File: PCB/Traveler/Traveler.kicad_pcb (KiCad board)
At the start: 2 copper layers, 5 parts, among them J1 Conn_01x06_motFL, J2 Conn_01x06_motFR, J3 Conn_01x06_motBL, J4 Conn_01x06_motBR, U1 ESP32-DEVKITC

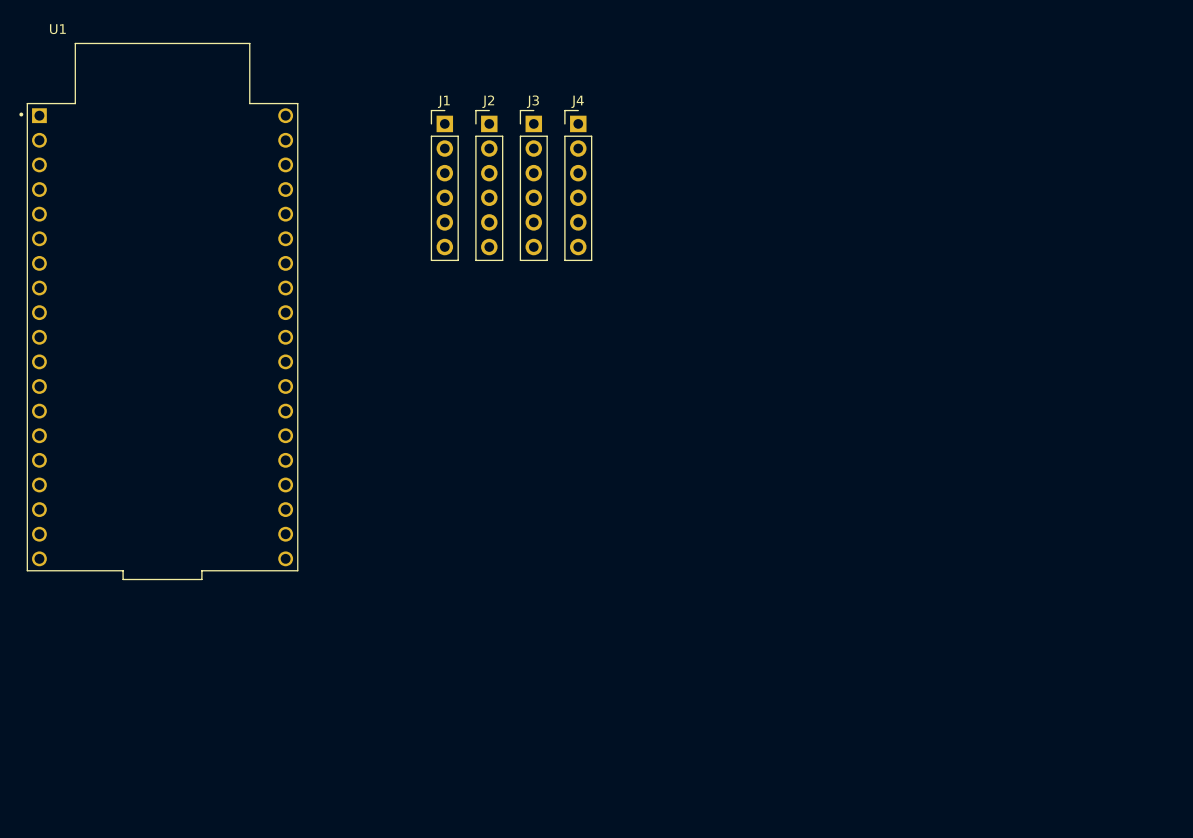
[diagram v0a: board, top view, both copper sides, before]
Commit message: Finition de pcb, prèt pour verification
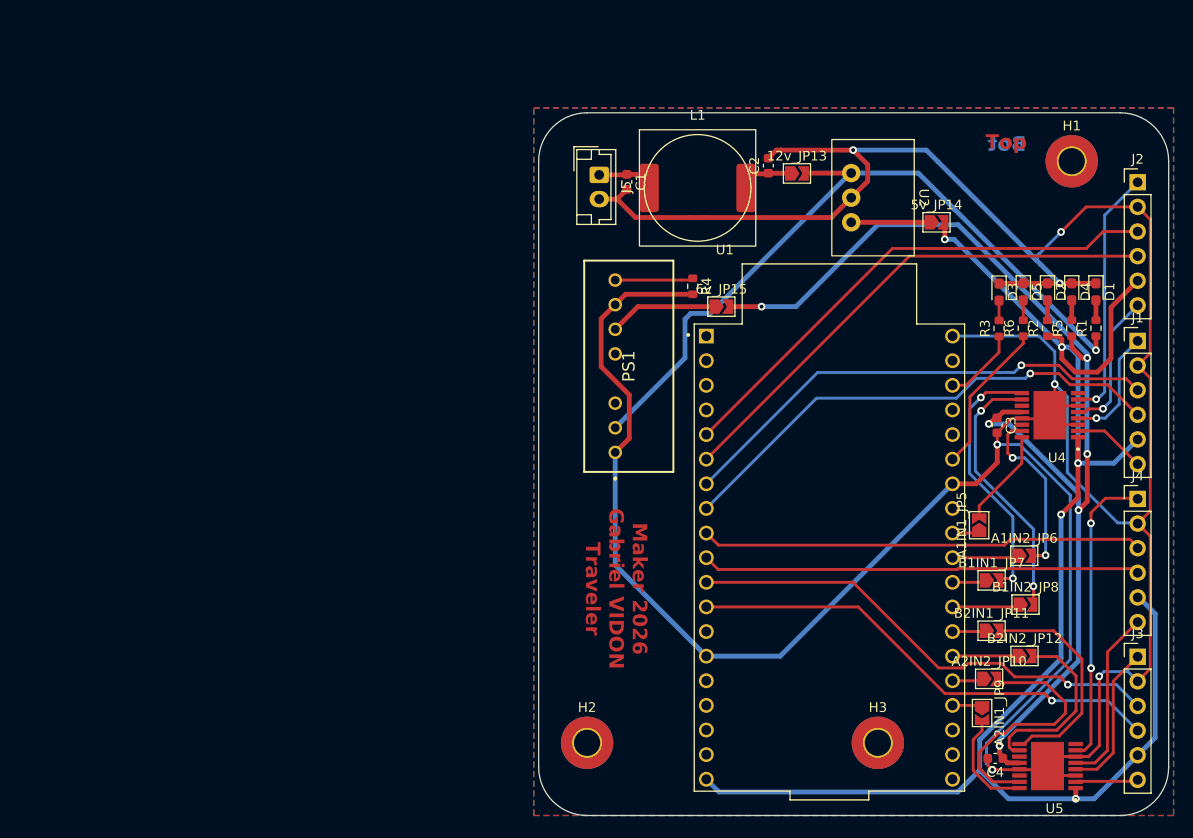
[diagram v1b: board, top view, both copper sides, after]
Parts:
- added 12v_JP13: SolderJumper_2_Open, Jumper:SolderJumper-2_P1.3mm_Open_TrianglePad1.0x1.5mm, F.Cu at (144.2, 48.8)
- added 5v_JP14: SolderJumper_2_Open, Jumper:SolderJumper-2_P1.3mm_Open_TrianglePad1.0x1.5mm, F.Cu at (158.5, 53.8)
- added 6v_JP15: SolderJumper_2_Open, Jumper:SolderJumper-2_P1.3mm_Open_TrianglePad1.0x1.5mm, F.Cu at (136.3, 62.5)
- added A1IN1_JP5: SolderJumper_2_Open, Jumper:SolderJumper-2_P1.3mm_Open_TrianglePad1.0x1.5mm, F.Cu at (162.9, 85.0)
- added A1IN2_JP6: SolderJumper_2_Open, Jumper:SolderJumper-2_P1.3mm_Open_TrianglePad1.0x1.5mm, F.Cu at (167.6, 88.2)
- added A2IN1_JP9: SolderJumper_2_Open, Jumper:SolderJumper-2_P1.3mm_Open_TrianglePad1.0x1.5mm, F.Cu at (163.2, 104.4)
- added A2IN2_JP10: SolderJumper_2_Open, Jumper:SolderJumper-2_P1.3mm_Open_TrianglePad1.0x1.5mm, F.Cu at (164.0, 100.9)
- added B1IN1_JP7: SolderJumper_2_Open, Jumper:SolderJumper-2_P1.3mm_Open_TrianglePad1.0x1.5mm, F.Cu at (164.2, 90.7)
- added B1IN2_JP8: SolderJumper_2_Open, Jumper:SolderJumper-2_P1.3mm_Open_TrianglePad1.0x1.5mm, F.Cu at (167.7, 93.2)
- added B2IN1_JP11: SolderJumper_2_Open, Jumper:SolderJumper-2_P1.3mm_Open_TrianglePad1.0x1.5mm, F.Cu at (164.2, 95.9)
- added B2IN2_JP12: SolderJumper_2_Open, Jumper:SolderJumper-2_P1.3mm_Open_TrianglePad1.0x1.5mm, F.Cu at (167.6, 98.5)
- added C1: 4.7u, Capacitor_SMD:C_0603_1608Metric, F.Cu at (126.6, 49.6)
- added C2: 4.7u, Capacitor_SMD:C_0603_1608Metric, F.Cu at (141.2, 48.0)
- added C3: 100n, Capacitor_SMD:C_0603_1608Metric, F.Cu at (164.8, 74.8)
- added C4: 100n, Capacitor_SMD:C_0603_1608Metric, F.Cu at (164.6, 109.1)
- added D1: LED_12v, LED_SMD:LED_0603_1608Metric_Pad1.05x0.95mm_HandSolder, F.Cu at (175.0, 61.0)
- added D2: LED_5v, LED_SMD:LED_0603_1608Metric_Pad1.05x0.95mm_HandSolder, F.Cu at (170.0, 61.0)
- added D3: LED_conn_bt, LED_SMD:LED_0603_1608Metric_Pad1.05x0.95mm_HandSolder, F.Cu at (165.0, 61.0)
- added D4: LED_6v, LED_SMD:LED_0603_1608Metric_Pad1.05x0.95mm_HandSolder, F.Cu at (172.5, 61.0)
- added D5: LED_spare1, LED_SMD:LED_0603_1608Metric_Pad1.05x0.95mm_HandSolder, F.Cu at (167.5, 61.0)
- added H1: MountingHole_Pad, MountingHole:MountingHole_2.7mm_Pad_TopBottom, F.Cu at (172.5, 47.5)
- added H2: MountingHole_Pad, MountingHole:MountingHole_2.7mm_Pad_TopBottom, F.Cu at (122.5, 107.5)
- added H3: MountingHole_Pad, MountingHole:MountingHole_2.7mm_Pad_TopBottom, F.Cu at (152.5, 107.5)
- added J5: Conn_batt, Connector_JST:JST_EH_B2B-EH-A_1x02_P2.50mm_Vertical, F.Cu at (123.8, 48.9)
- added L1: 10u, Capa:capa1, F.Cu at (133.9, 50.2)
- added PS1: 17791063215, 17791063215:17791063215, F.Cu at (125.4, 77.5)
- added R1: 4.7k, Resistor_SMD:R_0603_1608Metric, F.Cu at (175.0, 64.7)
- added R2: 1.2k, Resistor_SMD:R_0603_1608Metric, F.Cu at (170.0, 64.7)
- added R3: 120, Resistor_SMD:R_0603_1608Metric, F.Cu at (165.0, 64.7)
- added R4: 21.5k, Resistor_SMD:R_0603_1608Metric, F.Cu at (133.4, 60.4)
- added R5: 2.2k, Resistor_SMD:R_0603_1608Metric, F.Cu at (172.5, 64.7)
- added R6: 120, Resistor_SMD:R_0603_1608Metric, F.Cu at (167.5, 64.7)
- added U2: 12v-5v, Conv_dc-dc:173950x78, F.Cu at (159.7, 51.3)
- added U4: DRV8411APWPR, DRV8411APWPR:IC_DRV8411APWPR, F.Cu at (170.2, 73.7)
- added U5: DRV8411APWPR, DRV8411APWPR:IC_DRV8411APWPR, F.Cu at (170.0, 109.9)
- moved J3 83.1 mm to (179.3, 98.6)
- moved J1 74.9 mm to (179.3, 66.0)
- moved U1 72.5 mm to (147.5, 88.4)
- moved J4 69.5 mm to (179.3, 82.3)
- moved J2 67.2 mm to (179.3, 49.7)
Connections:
- J1 pad 1: unconnected-(J1-Pin_1-Pad1) -> /A1OUT2
- J1 pad 2: unconnected-(J1-Pin_2-Pad2) -> GND
- J1 pad 3: unconnected-(J1-Pin_3-Pad3) -> /Enc_A1_A
- J1 pad 4: unconnected-(J1-Pin_4-Pad4) -> /Enc_A1_B
- J1 pad 5: unconnected-(J1-Pin_5-Pad5) -> 5V
- J1 pad 6: unconnected-(J1-Pin_6-Pad6) -> /A1OUT1
- J2 pad 1: unconnected-(J2-Pin_1-Pad1) -> /B1OUT1
- J2 pad 2: unconnected-(J2-Pin_2-Pad2) -> GND
- J2 pad 3: unconnected-(J2-Pin_3-Pad3) -> /Enc_B1_A
- J2 pad 4: unconnected-(J2-Pin_4-Pad4) -> /Enc_B1_B
- J2 pad 5: unconnected-(J2-Pin_5-Pad5) -> 5V
- J2 pad 6: unconnected-(J2-Pin_6-Pad6) -> /B1OUT2
- J3 pad 1: unconnected-(J3-Pin_1-Pad1) -> /A2OUT2
- J3 pad 2: unconnected-(J3-Pin_2-Pad2) -> GND
- J3 pad 3: unconnected-(J3-Pin_3-Pad3) -> /Enc_A2_A
- J3 pad 4: unconnected-(J3-Pin_4-Pad4) -> /Enc_A2_B
- J3 pad 5: unconnected-(J3-Pin_5-Pad5) -> 5V
- J3 pad 6: unconnected-(J3-Pin_6-Pad6) -> /A2OUT1
- J4 pad 1: unconnected-(J4-Pin_1-Pad1) -> /B2OUT1
- J4 pad 2: unconnected-(J4-Pin_2-Pad2) -> GND
- J4 pad 3: unconnected-(J4-Pin_3-Pad3) -> /Enc_B2_A
- J4 pad 4: unconnected-(J4-Pin_4-Pad4) -> /Enc_B2_B
- J4 pad 5: unconnected-(J4-Pin_5-Pad5) -> 5V
- J4 pad 6: unconnected-(J4-Pin_6-Pad6) -> /B2OUT2
- U1 pad 10: unconnected-(U1-IO26-Pad10) -> /Enc_B2_B
- U1 pad 11: unconnected-(U1-IO27-Pad11) -> /Enc_A2_A
- U1 pad 12: unconnected-(U1-IO14-Pad12) -> /Enc_A2_B
- U1 pad 14: unconnected-(U1-GND1-Pad14) -> GND
- U1 pad 19: unconnected-(U1-EXT_5V-Pad19) -> 5V
- U1 pad 23: unconnected-(U1-IO15-Pad23) -> Net-(A2IN1_JP9-A)
- U1 pad 24: unconnected-(U1-IO2-Pad24) -> Net-(A2IN2_JP10-A)
- U1 pad 25: unconnected-(U1-IO0-Pad25) -> Net-(B2IN2_JP12-A)
- U1 pad 26: unconnected-(U1-IO4-Pad26) -> Net-(B2IN1_JP11-A)
- U1 pad 27: unconnected-(U1-IO16-Pad27) -> Net-(B1IN2_JP8-A)
- U1 pad 28: unconnected-(U1-IO17-Pad28) -> Net-(B1IN1_JP7-A)
- U1 pad 29: unconnected-(U1-IO5-Pad29) -> Net-(A1IN2_JP6-A)
- U1 pad 30: unconnected-(U1-IO18-Pad30) -> Net-(A1IN1_JP5-A)
- U1 pad 31: unconnected-(U1-IO19-Pad31) -> LED_spare2
- U1 pad 32: unconnected-(U1-GND2-Pad32) -> GND
- U1 pad 33: unconnected-(U1-IO21-Pad33) -> LED_spare1
- U1 pad 36: unconnected-(U1-IO22-Pad36) -> LED_conn_bt
- U1 pad 38: unconnected-(U1-GND3-Pad38) -> GND
- U1 pad 5: unconnected-(U1-IO34-Pad5) -> /Enc_B1_A
- U1 pad 6: unconnected-(U1-IO35-Pad6) -> /Enc_B1_B
- U1 pad 7: unconnected-(U1-IO32-Pad7) -> /Enc_A1_A
- U1 pad 8: unconnected-(U1-IO33-Pad8) -> /Enc_A1_B
- U1 pad 9: unconnected-(U1-IO25-Pad9) -> /Enc_B2_A
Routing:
- net GND: track 0.00 -> 360.0 mm, vias 0 -> 7
- net 5V: track 0.00 -> 164.3 mm, vias 0 -> 5
- net 6V: track 0.00 -> 114.7 mm, vias 0 -> 6
- net 12V: track 0.00 -> 76.6 mm, vias 0 -> 1
- net /Enc_B1_A: track 0.00 -> 53.2 mm
- net /Enc_B1_B: track 0.00 -> 53.2 mm
- net /Enc_A1_B: track 0.00 -> 52.0 mm, vias 0 -> 1
- net /Enc_A1_A: track 0.00 -> 50.6 mm, vias 0 -> 1
- net /Enc_A2_A: track 0.00 -> 50.2 mm, vias 0 -> 1
- net /Enc_A2_B: track 0.00 -> 49.8 mm, vias 0 -> 1
- net /Enc_B2_A: track 0.00 -> 45.7 mm
- net /Enc_B2_B: track 0.00 -> 45.2 mm
- net /B2OUT1: track 0.00 -> 31.2 mm, vias 0 -> 2
- net B1IN2: track 0.00 -> 27.4 mm, vias 0 -> 2
- net B1IN1: track 0.00 -> 27.0 mm, vias 0 -> 2
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- added copper zone on B.Cu, net GND
- added copper zone on F.Cu, net GND
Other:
- board outline added: 65 x 72.5 mm
- board text added: "Bot"
- board text added: "Maker 2026 Gabriel VIDON Traveler"
- board text added: "Top"

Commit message: Vers 2 couches
A créer : une vers 4 couches, remplacer batt 12v vers 6v pour alim directement depuis batt
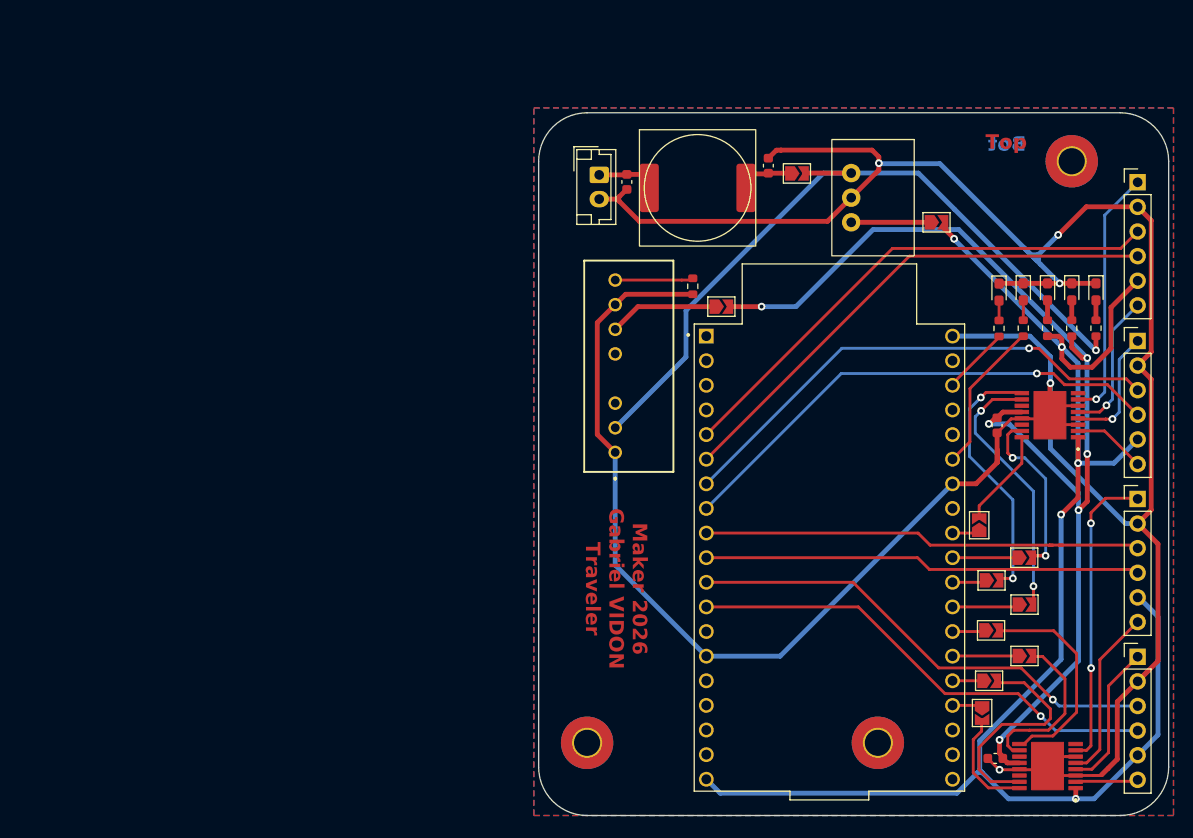
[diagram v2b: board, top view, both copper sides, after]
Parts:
- moved A1IN2_JP6 0.20 mm to (167.6, 88.4)
- moved A2IN2_JP10 0.20 mm to (164.0, 101.1)
- moved B1IN2_JP8 0.10 mm to (167.6, 93.2)
- moved B2IN1_JP11 0.07 mm to (164.2, 95.9)
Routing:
- net GND: track 360.0 -> 323.9 mm, vias 7 -> 5
- net A2IN2: track 26.0 -> 23.1 mm
- net B2IN2: track 19.3 -> 17.3 mm
- net A1IN2: track 17.9 -> 19.5 mm
- net /Enc_A1_A: track 50.6 -> 52.1 mm
- net 5V: track 164.3 -> 163.3 mm
- net B2IN1: track 23.2 -> 22.3 mm
- net LED_conn_bt: track 7.84 -> 7.03 mm
- net 6V: track 114.7 -> 114.0 mm
- net /B2OUT2: track 18.4 -> 17.9 mm
